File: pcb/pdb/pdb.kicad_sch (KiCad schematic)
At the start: 12 parts

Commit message: chore: add circuit git changes
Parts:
- removed C? (x2): 10u, symbol Device:C_Small
- removed D? (x2): SS2040, Diode_SMD:D_MELF, symbol Diode:1N5712UR
- removed D?: LED, symbol Device:LED
- removed J? (x3): Conn_01x02_Male, symbol Connector:Conn_01x02_Male
- removed J? (x2): Conn_01x02_Female, symbol Connector:Conn_01x02_Female
- removed R?: 1k, symbol Device:R_Small
- removed U?: R-78E5.0-0.5, symbol bldc_lib:R-78E5.0-0.5
- added J1, J2, J3, J4: Conn_01x02, Connector_AMASS:AMASS_XT30U-M_1x02_P5.0mm_Vertical, symbol Connector_Generic:Conn_01x02
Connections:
- net +BATT: now also J1.2 (Pin_2), J2.2 (Pin_2), J3.2 (Pin_2), J4.2 (Pin_2)
- net GND: now also J1.1 (Pin_1), J2.1 (Pin_1), J3.1 (Pin_1), J4.1 (Pin_1)

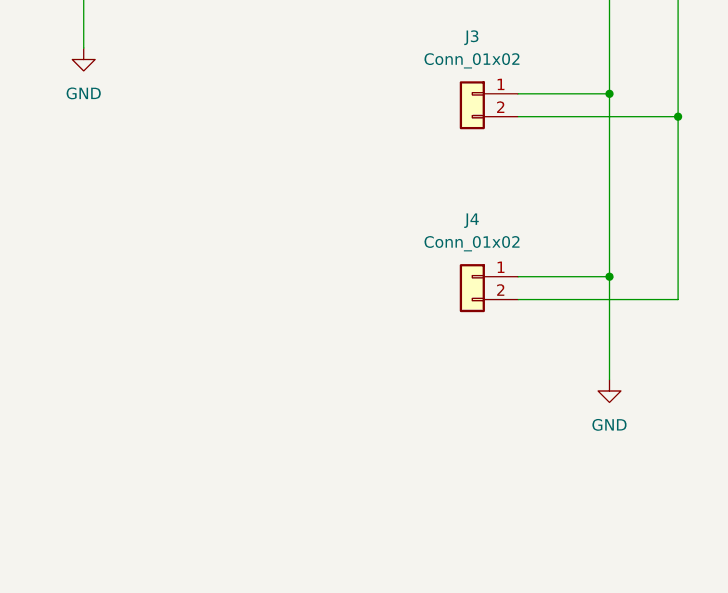
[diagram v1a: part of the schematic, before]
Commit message: feat: finish adding a connector
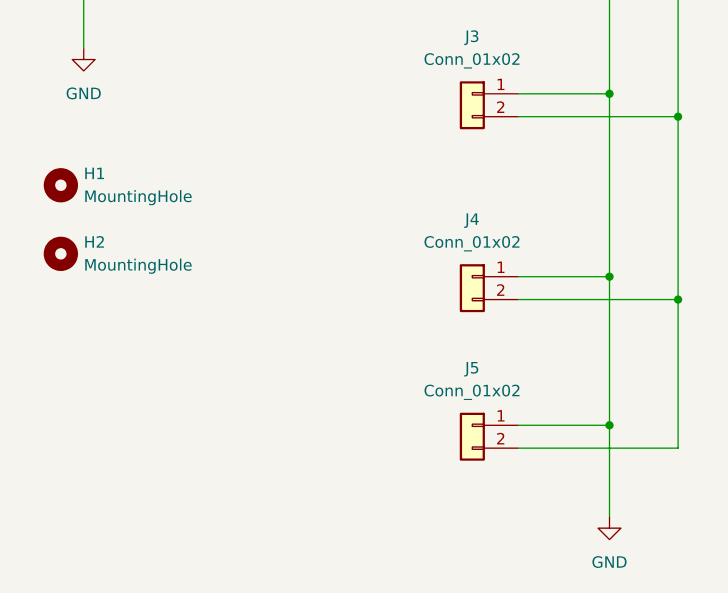
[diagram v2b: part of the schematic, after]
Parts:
- added H1, H2: MountingHole, MountingHole:MountingHole_3.2mm_M3_Pad_TopBottom, symbol Mechanical:MountingHole
- added J5: Conn_01x02, Connector_AMASS:AMASS_XT30U-M_1x02_P5.0mm_Vertical, symbol Connector_Generic:Conn_01x02
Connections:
- net +BATT: now also J5.2 (Pin_2)
- net GND: now also J5.1 (Pin_1)

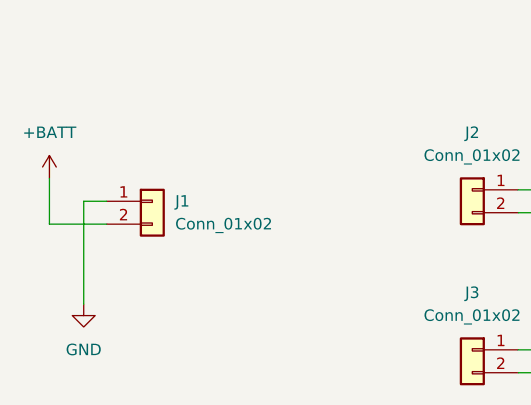
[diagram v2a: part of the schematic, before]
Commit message: feat: add DC jack & change XT30 footprint
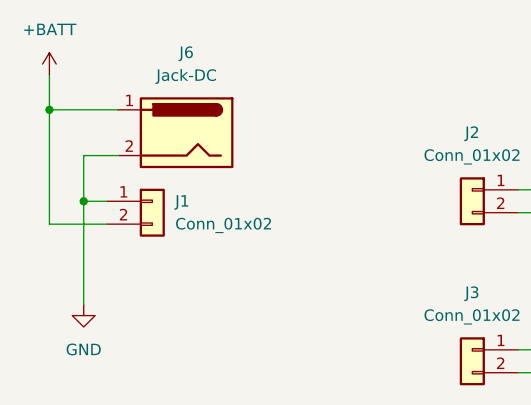
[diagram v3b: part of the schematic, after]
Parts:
- added J6: Jack-DC, Connector_BarrelJack:BarrelJack_Horizontal, symbol Connector:Jack-DC
- J1, J2, J3, J4, J5: footprint Connector_AMASS:AMASS_XT30U-M_1x02_P5.0mm_Vertical -> Connector_AMASS:AMASS_XT30PW-M_1x02_P2.50mm_Horizontal
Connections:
- net +BATT: now also J6.1
- net GND: now also J6.2
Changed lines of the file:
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@@
+	)
+	(junction
+		(at 100.33 62.23)
+		(diameter 0)
+		(color 0 0 0 0)
+	)
+	(junction
+		(at 104.14 72.39)
+		(diameter 0)
+		(color 0 0 0 0)
 	)
 	(junction
@@
 	(wire
 		(pts
-			(xy 100.33 74.93) (xy 100.33 69.85)
+			(xy 100.33 74.93) (xy 100.33 62.23)
 		)
 		(stroke
@@
 	(wire
 		(pts
+			(xy 104.14 67.31) (xy 104.14 72.39)
+		)
+		(stroke
+			(width 0)
+			(type default)
+		)
+	)
+	(wire
+		(pts
 			(xy 162.56 71.12) (xy 162.56 88.9)
 		)
@@
 	(wire
 		(pts
+			(xy 100.33 62.23) (xy 100.33 58.42)
+		)
+		(stroke
+			(width 0)
+			(type default)
+		)
+	)
+	(wire
+		(pts
 			(xy 152.4 88.9) (xy 162.56 88.9)
 		)
@@
 		(pts
 			(xy 170.18 73.66) (xy 170.18 91.44)
+		)
+		(stroke
+			(width 0)
+			(type default)
+		)
+	)
+	(wire
+		(pts
+			(xy 107.95 67.31) (xy 104.14 67.31)
+		)
+		(stroke
+			(width 0)
+			(type default)
+		)
+	)
+	(wire
+		(pts
+			(xy 100.33 62.23) (xy 107.95 62.23)
 		)
 		(stroke
@@
 			)
 		)
-		(property "Footprint" "Connector_AMASS:AMASS_XT30U-M_1x02_P5.0mm_Vertical"
+		(property "Footprint" "Connector_AMASS:AMASS_XT30PW-M_1x02_P2.50mm_Horizontal"
 			(at 147.32 109.22 0)
 			(effects
@@
 			)
 		)
-		(property "Footprint" "Connector_AMASS:AMASS_XT30U-M_1x02_P5.0mm_Vertical"
+		(property "Footprint" "Connector_AMASS:AMASS_XT30PW-M_1x02_P2.50mm_Horizontal"
 			(at 147.32 71.12 0)
 			(effects
@@
 	)
 	(symbol
+		(lib_id "Connector:Jack-DC")
+		(at 115.57 64.77 0)
+		(mirror y)
+		(unit 1)
+		(exclude_from_sim no)
+		(in_bom yes)
+		(on_board yes)
+		(dnp no)
+		(property "Reference" "J6"
+			(at 115.57 55.88 0)
+			(effects
+				(font
+					(size 1.27 1.27)
+				)
+			)
+		)
+		(property "Value" "Jack-DC"
+			(at 115.57 58.42 0)
+			(effects
+				(font
+					(size 1.27 1.27)
+				)
+			)
+		)
+		(property "Footprint" "Connector_BarrelJack:BarrelJack_Horizontal"
+			(at 114.3 65.786 0)
+			(effects
+				(font
+					(size 1.27 1.27)
+				)
+				(hide yes)
+			)
+		)
+		(property "Datasheet" "~"
+			(at 114.3 65.786 0)
+			(effects
+				(font
+					(size 1.27 1.27)
+				)
+				(hide yes)
+			)
+		)
+		(property "Description" "DC Barrel Jack"
+			(at 115.57 64.77 0)
+			(effects
+				(font
+					(size 1.27 1.27)
+				)
+				(hide yes)
+			)
+		)
+		(pin "2"
+		)
+		(pin "1"
+		)
+		(instances
+			(project ""
+				(path "/995b6394-4c8f-4995-8552-0d233dbcf3a4"
+					(reference "J6")
+					(unit 1)
+				)
+			)
+		)
+	)
+	(symbol
 		(lib_id "power:GND")
 		(at 162.56 135.89 0)
@@
 	(symbol
 		(lib_id "power:+BATT")
-		(at 100.33 69.85 0)
+		(at 100.33 58.42 0)
 		(unit 1)
 		(exclude_from_sim no)
@@
 		(fields_autoplaced yes)
 		(property "Reference" "#PWR01"
-			(at 100.33 73.66 0)
+			(at 100.33 62.23 0)
 			(effects
 				(font
@@
 		)
 		(property "Value" "+BATT"
-			(at 100.33 64.77 0)
+			(at 100.33 53.34 0)
 			(effects
 				(font
@@
 		)
 		(property "Footprint" ""
-			(at 100.33 69.85 0)
+			(at 100.33 58.42 0)
 			(effects
 				(font
@@
 		)
 		(property "Datasheet" ""
-			(at 100.33 69.85 0)
+			(at 100.33 58.42 0)
 			(effects
 				(font
@@
 		)
 		(property "Description" ""
-			(at 100.33 69.85 0)
+			(at 100.33 58.42 0)
 			(effects
 				(font
@@
 			)
 		)
-		(property "Footprint" "Connector_AMASS:AMASS_XT30U-M_1x02_P5.0mm_Vertical"
+		(property "Footprint" "Connector_AMASS:AMASS_XT30PW-M_1x02_P2.50mm_Horizontal"
 			(at 147.32 125.73 0)
 			(effects
@@
 			)
 		)
-		(property "Footprint" "Connector_AMASS:AMASS_XT30U-M_1x02_P5.0mm_Vertical"
+		(property "Footprint" "Connector_AMASS:AMASS_XT30PW-M_1x02_P2.50mm_Horizontal"
 			(at 111.76 72.39 0)
 			(effects
@@
 			)
 		)
-		(property "Footprint" "Connector_AMASS:AMASS_XT30U-M_1x02_P5.0mm_Vertical"
+		(property "Footprint" "Connector_AMASS:AMASS_XT30PW-M_1x02_P2.50mm_Horizontal"
 			(at 147.32 88.9 0)
 			(effects
